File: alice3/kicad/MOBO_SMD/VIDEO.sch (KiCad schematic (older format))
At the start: 17 parts, among them J1 VGA, P1 CONN_01X05, SW1 RESET, U2 Propeller_P8X32A-Q44, U3 24LC256, U4 Propeller_Plug, Y1 5 MHz

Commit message: Fix some footprint assignments.
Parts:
- J1: footprint (none) -> Jac:00JG-DB15HDSOCKET
- SW1: footprint Buttons_Switches_ThroughHole:SW_PUSH_SMALL -> Buttons_Switches_SMD:SW_SPST_PTS645
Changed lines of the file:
@@
 F 0 "SW1" H 6050 1560 50  0000 C CNN
 F 1 "RESET" H 5900 1370 50  0000 C CNN
-F 2 "Buttons_Switches_ThroughHole:SW_PUSH_SMALL" H 5900 1450 50  0001 C CNN
+F 2 "Buttons_Switches_SMD:SW_SPST_PTS645" H 5900 1450 50  0001 C CNN
 F 3 "" H 5900 1450 50  0000 C CNN
 	1    5900 1450
@@
 F 0 "J1" H 3800 6975 60  0000 C CNN
 F 1 "VGA" H 4050 5425 60  0000 C CNN
-F 2 "" H 4050 6175 60  0001 C CNN
+F 2 "Jac:00JG-DB15HDSOCKET" H 4050 6175 60  0001 C CNN
 F 3 "" H 4050 6175 60  0000 C CNN
 	1    4050 6175

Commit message: Switch to new MicroSD footprint and new Prop crystal.
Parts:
- Y1: footprint Crystals:Crystal_HC49-SD_SMD -> Crystals:Crystal_HC50-U_Vertical
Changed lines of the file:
@@
 F 0 "Y1" H 5350 3750 50  0000 C CNN
 F 1 "5 MHz" H 5350 3450 50  0000 C CNN
-F 2 "Crystals:Crystal_HC49-SD_SMD" H 5350 3600 50  0001 C CNN
+F 2 "Crystals:Crystal_HC50-U_Vertical" H 5350 3600 50  0001 C CNN
 F 3 "" H 5350 3600 50  0000 C CNN
 	1    5350 3600

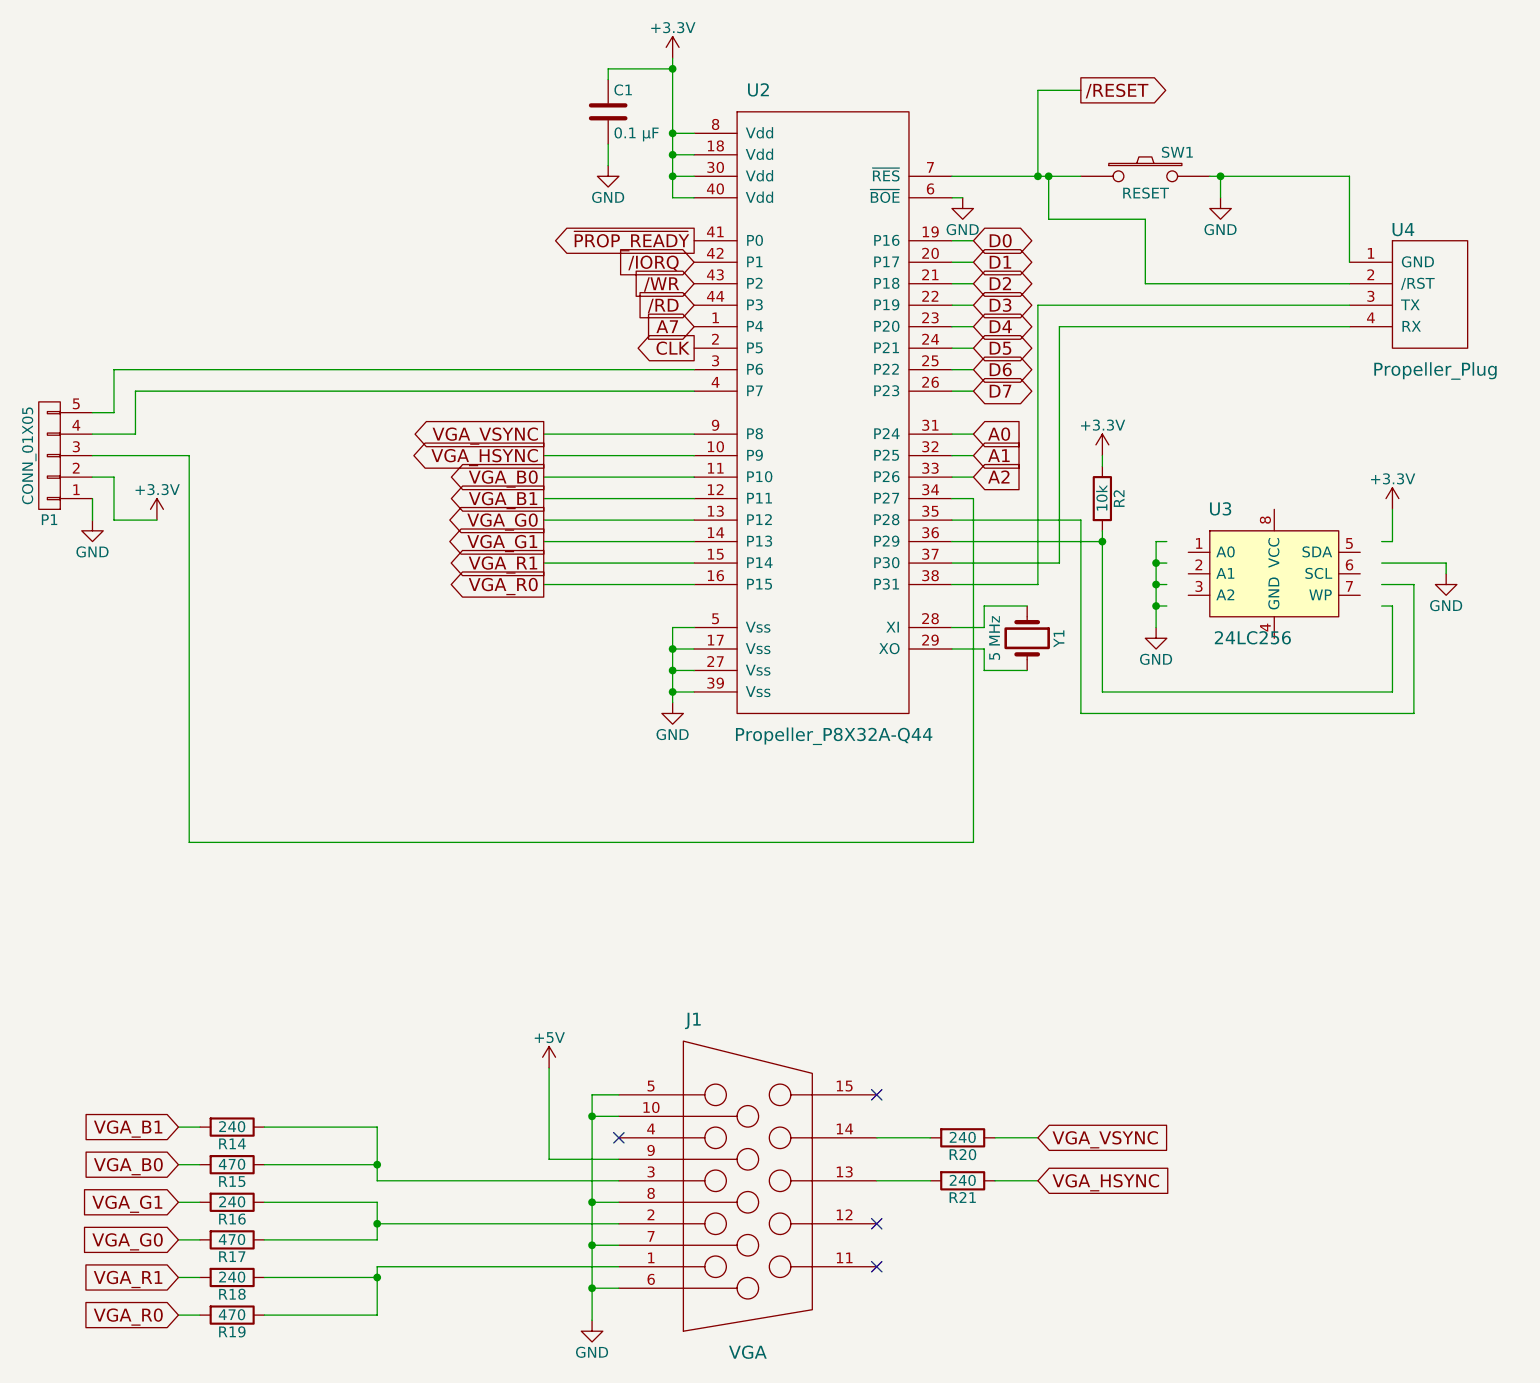
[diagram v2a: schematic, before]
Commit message: 1st set MOBO schematic fixes for 1st PCBWay spin
Various fixes for KiCAD messing up components

Button on BOOT0

No huge cap on power supply LED

Discard RAM

Route ARM to Z80 /WAIT and /RFSH

Use "~" for active-low lines (shown in schematic by line above them)
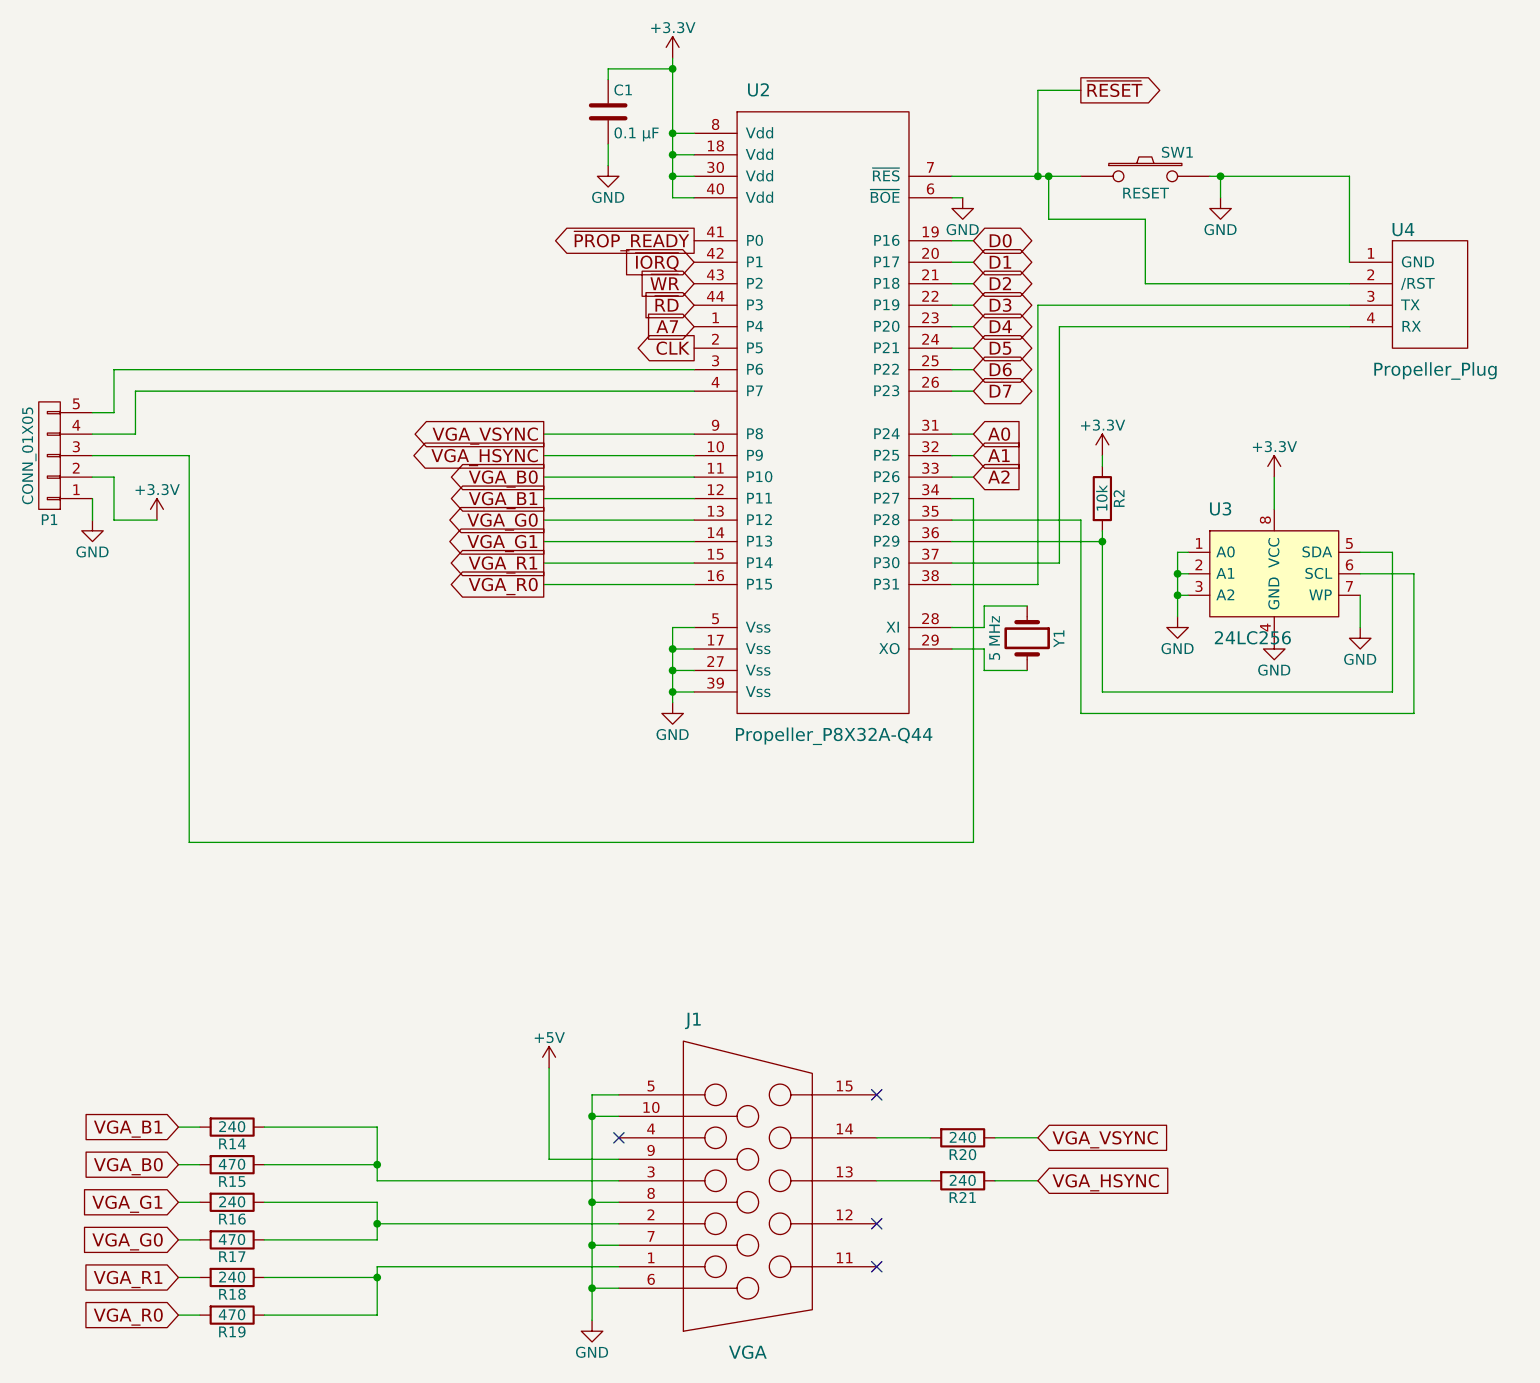
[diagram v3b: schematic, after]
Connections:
- net labels added: ~IORQ, ~RD, ~RESET, ~WR
- net labels removed: /IORQ, /RD, /RESET, /WR
- wire segments 120 -> 117
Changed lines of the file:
@@
 L GND #PWR04
 U 1 1 5681F164
-P 5950 3550
-F 0 "#PWR04" H 5950 3300 50  0001 C CNN
-F 1 "GND" H 5950 3400 50  0000 C CNN
-F 2 "" H 5950 3550 50  0000 C CNN
-F 3 "" H 5950 3550 50  0000 C CNN
-	1    5950 3550
+P 6050 3500
+F 0 "#PWR04" H 6050 3250 50  0001 C CNN
+F 1 "GND" H 6050 3350 50  0000 C CNN
+F 2 "" H 6050 3500 50  0000 C CNN
+F 3 "" H 6050 3500 50  0000 C CNN
+	1    6050 3500
 	1    0    0    -1
 $EndComp
@@
 L +3.3V #PWR05
 U 1 1 5681F2C2
-P 7050 3000
-F 0 "#PWR05" H 7050 2850 50  0001 C CNN
-F 1 "+3.3V" H 7050 3140 50  0000 C CNN
-F 2 "" H 7050 3000 50  0000 C CNN
-F 3 "" H 7050 3000 50  0000 C CNN
-	1    7050 3000
+P 6500 2850
+F 0 "#PWR05" H 6500 2700 50  0001 C CNN
+F 1 "+3.3V" H 6500 2990 50  0000 C CNN
+F 2 "" H 6500 2850 50  0000 C CNN
+F 3 "" H 6500 2850 50  0000 C CNN
+	1    6500 2850
 	1    0    0    -1
 $EndComp
@@
 L GND #PWR06
 U 1 1 5681F2E8
-P 7300 3300
-F 0 "#PWR06" H 7300 3050 50  0001 C CNN
-F 1 "GND" H 7300 3150 50  0000 C CNN
-F 2 "" H 7300 3300 50  0000 C CNN
-F 3 "" H 7300 3300 50  0000 C CNN
-	1    7300 3300
+P 6500 3600
+F 0 "#PWR06" H 6500 3350 50  0001 C CNN
+F 1 "GND" H 6500 3450 50  0000 C CNN
+F 2 "" H 6500 3600 50  0000 C CNN
+F 3 "" H 6500 3600 50  0000 C CNN
+	1    6500 3600
 	1    0    0    -1
 $EndComp
@@
 	3100 3350 3800 3350
 Wire Wire Line
-	6000 3150 5950 3150
-Wire Wire Line
-	5950 3150 5950 3550
-Wire Wire Line
-	6000 3250 5950 3250
-Connection ~ 5950 3250
-Wire Wire Line
-	6000 3350 5950 3350
-Connection ~ 5950 3350
-Wire Wire Line
-	6000 3450 5950 3450
-Connection ~ 5950 3450
-Wire Wire Line
-	7000 3150 7050 3150
-Wire Wire Line
-	7050 3150 7050 3000
-Wire Wire Line
-	7000 3250 7300 3250
-Wire Wire Line
-	7300 3250 7300 3300
-Wire Wire Line
-	7000 3350 7150 3350
-Wire Wire Line
-	7150 3350 7150 3950
+	6100 3200 6050 3200
+Wire Wire Line
+	6100 3300 6050 3300
+Connection ~ 6050 3300
+Wire Wire Line
+	6100 3400 6050 3400
+Connection ~ 6050 3400
+Wire Wire Line
+	6500 3000 6500 2850
+Wire Wire Line
+	7150 3300 7150 3950
 Wire Wire Line
 	7150 3950 5600 3950
@@
 	5600 3050 5000 3050
 Wire Wire Line
-	7000 3450 7050 3450
-Wire Wire Line
-	7050 3450 7050 3850
+	7050 3200 7050 3850
 Wire Wire Line
 	7050 3850 5700 3850
@@
 D7
 Text GLabel 3800 1850 0    60   Input ~ 0
-/IORQ
+~IORQ
 Text GLabel 3800 1950 0    60   Input ~ 0
-/WR
+~WR
 Text GLabel 3800 2150 0    60   Input ~ 0
 A7
 Text GLabel 3800 2050 0    60   Input ~ 0
-/RD
+~RD
 $Comp
 L C C1
@@
 	5000 2850 5100 2850
 Text GLabel 5600 1050 2    60   Output ~ 0
-/RESET
+~RESET
 Wire Wire Line
 	5400 1050 5600 1050
@@
 Text GLabel 3800 1750 0    60   Output ~ 0
 ~PROP_READY~
+Wire Wire Line
+	6050 3200 6050 3500
+Wire Wire Line
+	7150 3300 6900 3300
+Wire Wire Line
+	7050 3200 6900 3200
+$Comp
+L GND #PWR014
+U 1 1 59A44AF1
+P 6900 3550
+F 0 "#PWR014" H 6900 3300 50  0001 C CNN
+F 1 "GND" H 6900 3400 50  0000 C CNN
+F 2 "" H 6900 3550 50  0000 C CNN
+F 3 "" H 6900 3550 50  0000 C CNN
+	1    6900 3550
+	1    0    0    -1
+$EndComp
+Wire Wire Line
+	6900 3400 6900 3550
 $EndSCHEMATC

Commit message: change Prop crystal to SMT
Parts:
- Y1: footprint Crystals:Crystal_HC50-U_Vertical -> Crystals:Crystal_HC49-SD_SMD; Part (none) -> https://www.digikey.com/product-detail/en/ecs-inc/ECS-50-20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
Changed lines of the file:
@@
 F 0 "Y1" H 5350 3750 50  0000 C CNN
 F 1 "5 MHz" H 5350 3450 50  0000 C CNN
-F 2 "Crystals:Crystal_HC50-U_Vertical" H 5350 3600 50  0001 C CNN
+F 2 "Crystals:Crystal_HC49-SD_SMD" H 5350 3600 50  0001 C CNN
 F 3 "" H 5350 3600 50  0000 C CNN
+F 4 "https://www.digikey.com/product-detail/en/ecs-inc/ECS-50-20-5PX-TR/XC1265CT-ND/827729" H 5350 3600 60  0001 C CNN "Part"
 	1    5350 3600
 	0    1    1    0

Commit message: fix inductor, fix HOME
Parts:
- J1: Distributor (none) -> Digikey; Distributor PN (none) -> A35119-ND; Manufacturer (none) -> TE Connectivity AMP Connectors; PN (none) -> 1734344-1
- P1: Distributor (none) -> Digikey; Distributor PN (none) -> 929500E-01-05-ND; Manufacturer (none) -> 3M; PN (none) -> 929500-01-05-RK
- SW1: Distributor (none) -> Digikey; Distributor PN (none) -> CKN9085CT-ND; Manufacturer (none) -> C&K; PN (none) -> PTS645SH50SMTR92
- U2: Distributor (none) -> Digikey; Distributor PN (none) -> P8X32A-Q44-ND; Manufacturer (none) -> Parallax Inc.; PN (none) -> P8X32A-Q44
- U3: Distributor (none) -> Digikey; Distributor PN (none) -> 24LC256T-I/SNCT-ND; Manufacturer (none) -> Microchip Technology TECHNOLOGY; PN (none) -> 24LC256T-I/SN
- U4: Distributor (none) -> Digikey; Distributor PN (none) -> 929500E-01-04-ND; Manufacturer (none) -> 3M; PN (none) -> 929500-01-04-RK
- Y1: Distributor (none) -> Digikey; Distributor PN (none) -> XC1265CT-ND; Manufacturer (none) -> ECS Inc.; PN (none) -> ECS-50-20-5PX-TR; Part https://www.digikey.com/product-detail/en/ecs-inc/ECS-50-20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 -> (none)
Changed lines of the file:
@@
 LIBS:propeller_p8x32a-q44
 LIBS:as6c2008_tsop
+LIBS:conn-fci
 LIBS:MOBO_SMD-cache
 EELAYER 25 0
@@
 F 2 "Crystals:Crystal_HC49-SD_SMD" H 5350 3600 50  0001 C CNN
 F 3 "" H 5350 3600 50  0000 C CNN
-F 4 "https://www.digikey.com/product-detail/en/ecs-inc/ECS-50-20-5PX-TR/XC1265CT-ND/827729" H 5350 3600 60  0001 C CNN "Part"
+F 4 "ECS Inc." H 975 3575 60  0001 C CNN "Manufacturer"
+F 5 "ECS-50-20-5PX-TR" H 975 3575 60  0001 C CNN "PN"
+F 6 "Digikey" H 975 3575 60  0001 C CNN "Distributor"
+F 7 "XC1265CT-ND" H 975 3575 60  0001 C CNN "Distributor PN"
 	1    5350 3600
 	0    1    1    0
@@
 F 2 "Buttons_Switches_SMD:SW_SPST_PTS645" H 5900 1450 50  0001 C CNN
 F 3 "" H 5900 1450 50  0000 C CNN
+F 4 "C&K" H 975 3575 60  0001 C CNN "Manufacturer"
+F 5 "PTS645SH50SMTR92" H 975 3575 60  0001 C CNN "PN"
+F 6 "Digikey" H 975 3575 60  0001 C CNN "Distributor"
+F 7 "CKN9085CT-ND" H 975 3575 60  0001 C CNN "Distributor PN"
 	1    5900 1450
 	1    0    0    -1
@@
 F 2 "Housings_SOIC:SOIC-8_3.9x4.9mm_Pitch1.27mm" H 6500 3200 60  0001 C CNN
 F 3 "" H 6500 3200 60  0000 C CNN
+F 4 "Microchip Technology TECHNOLOGY" H 975 3575 60  0001 C CNN "Manufacturer"
+F 5 "24LC256T-I/SN" H 975 3575 60  0001 C CNN "PN"
+F 6 "Digikey" H 975 3575 60  0001 C CNN "Distributor"
+F 7 "24LC256T-I/SNCT-ND" H 975 3575 60  0001 C CNN "Distributor PN"
 	1    6500 3300
 	1    0    0    -1
@@
 F 2 "Pin_Headers:Pin_Header_Angled_1x04" H 7200 2000 60  0001 C CNN
 F 3 "" H 7200 2000 60  0000 C CNN
+F 4 "3M" H 975 3575 60  0001 C CNN "Manufacturer"
+F 5 "929500-01-04-RK" H 975 3575 60  0001 C CNN "PN"
+F 6 "Digikey" H 975 3575 60  0001 C CNN "Distributor"
+F 7 "929500E-01-04-ND" H 975 3575 60  0001 C CNN "Distributor PN"
 	1    7200 2000
 	1    0    0    -1
@@
 F 2 "Pin_Headers:Pin_Header_Angled_1x05" H 800 2750 50  0001 C CNN
 F 3 "" H 800 2750 50  0000 C CNN
+F 4 "3M" H 975 3575 60  0001 C CNN "Manufacturer"
+F 5 "929500-01-05-RK" H 975 3575 60  0001 C CNN "PN"
+F 6 "Digikey" H 975 3575 60  0001 C CNN "Distributor"
+F 7 "929500E-01-05-ND" H 975 3575 60  0001 C CNN "Distributor PN"
 	1    800  2750
 	-1   0    0    1
@@
 F 2 "Jac:00JG-DB15HDSOCKET" H 4050 6175 60  0001 C CNN
 F 3 "" H 4050 6175 60  0000 C CNN
+F 4 "TE Connectivity AMP Connectors" H 975 3575 60  0001 C CNN "Manufacturer"
+F 5 "1734344-1" H 975 3575 60  0001 C CNN "PN"
+F 6 "Digikey" H 975 3575 60  0001 C CNN "Distributor"
+F 7 "A35119-ND" H 975 3575 60  0001 C CNN "Distributor PN"
 	1    4050 6175
 	1    0    0    -1
@@
 F 2 "Housings_QFP:LQFP-44_10x10mm_Pitch0.8mm" H 4400 2350 60  0001 C CNN
 F 3 "" H 4400 2350 60  0000 C CNN
+F 4 "Parallax Inc." H 975 3575 60  0001 C CNN "Manufacturer"
+F 5 "P8X32A-Q44" H 975 3575 60  0001 C CNN "PN"
+F 6 "Digikey" H 975 3575 60  0001 C CNN "Distributor"
+F 7 "P8X32A-Q44-ND" H 975 3575 60  0001 C CNN "Distributor PN"
 	1    4400 2550
 	1    0    0    -1
